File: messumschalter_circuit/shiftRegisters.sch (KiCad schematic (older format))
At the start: 24 parts

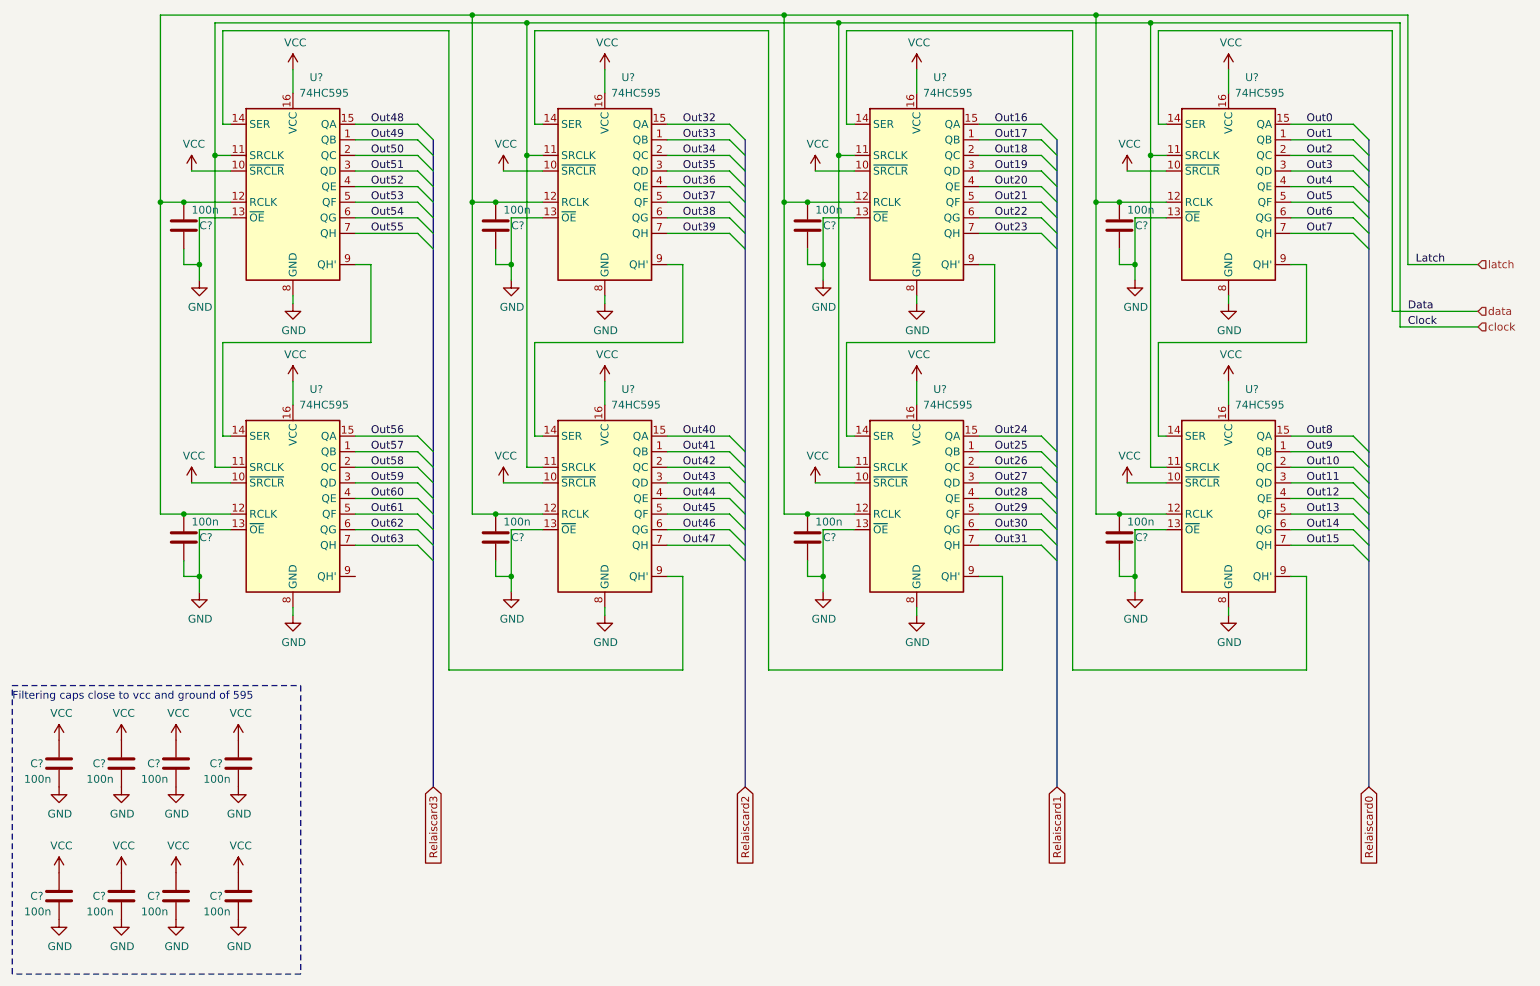
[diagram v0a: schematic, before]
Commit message: reduce to double 595 per board, leds and dip
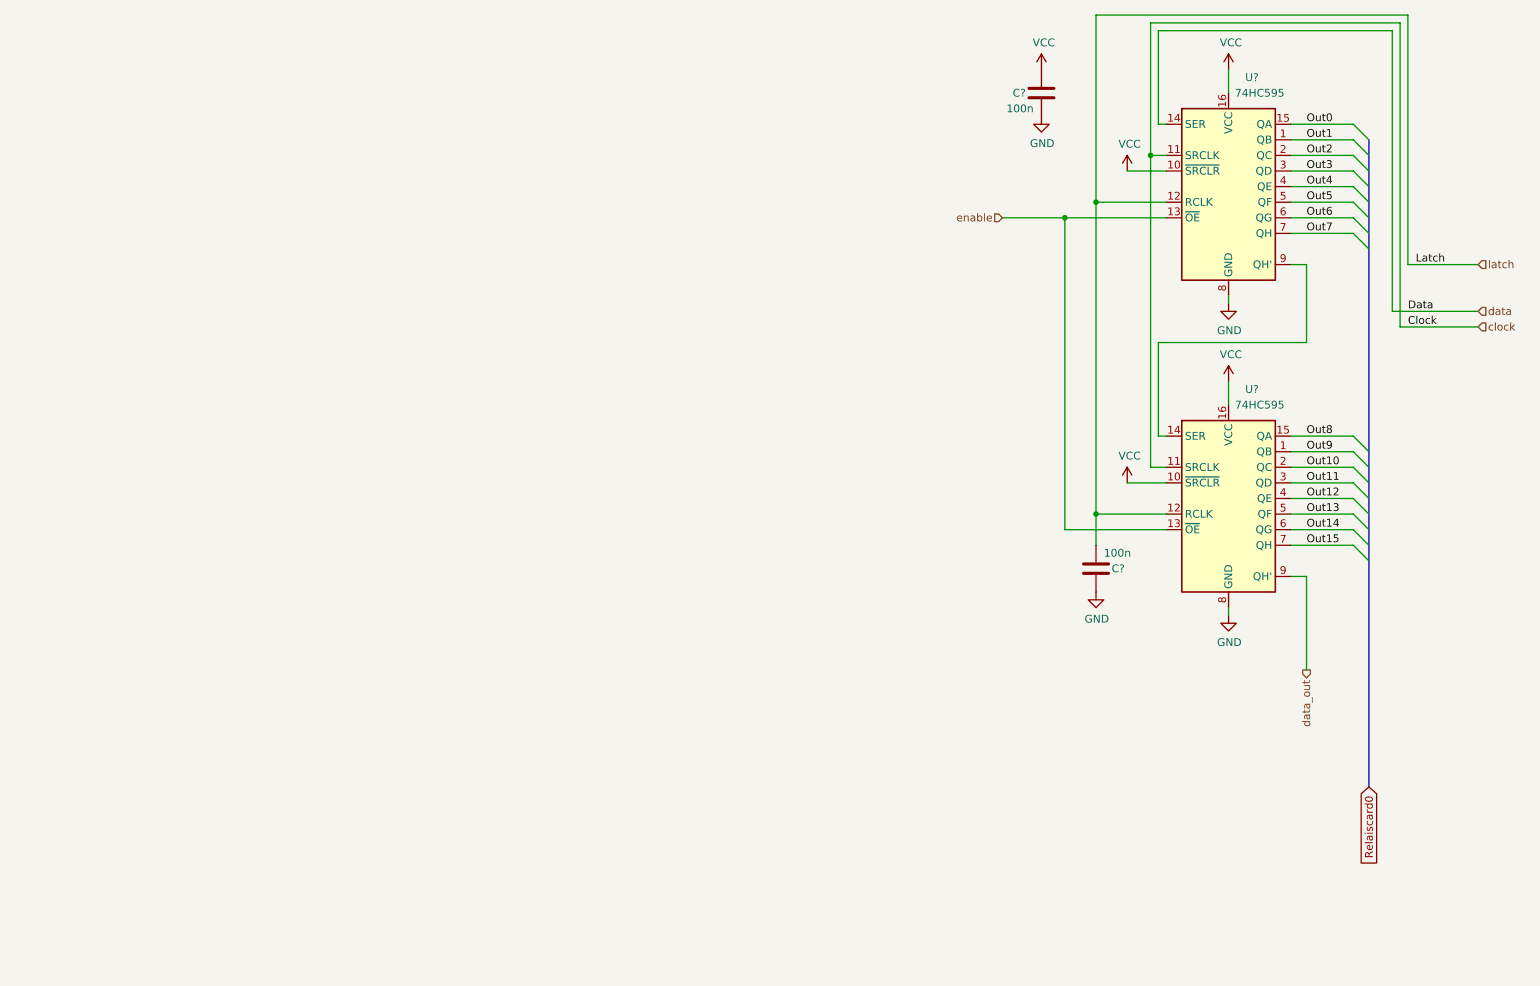
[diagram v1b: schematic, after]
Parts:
- removed C? (x14): 100n, symbol Device:C
- removed U? (x6): 74HC595, symbol 74xx:74HC595
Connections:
- net GND: no longer U?.13 (~OE), U?.13 (~OE)
- net data_out: now reaches U?.9 (QH')
- new net enable: U?.13 (~OE), U?.13 (~OE)
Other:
- note removed: "Filtering caps close to vcc and ground of 595"
- moved on the sheet: C?
